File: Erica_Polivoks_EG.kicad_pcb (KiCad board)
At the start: 2 copper layers, 40.3 x 106 mm, 92 parts, among them J1 GATE IN, J2 INV EG OUT, J3 Eurorack_Power_10pin_Unshroud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, J4 GATE DELAY OUT, J5 EG OUT, Q1 2N3904, Q2 2N3904, Q3 2N3904, Q4 2N3904, Q5 2N3904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

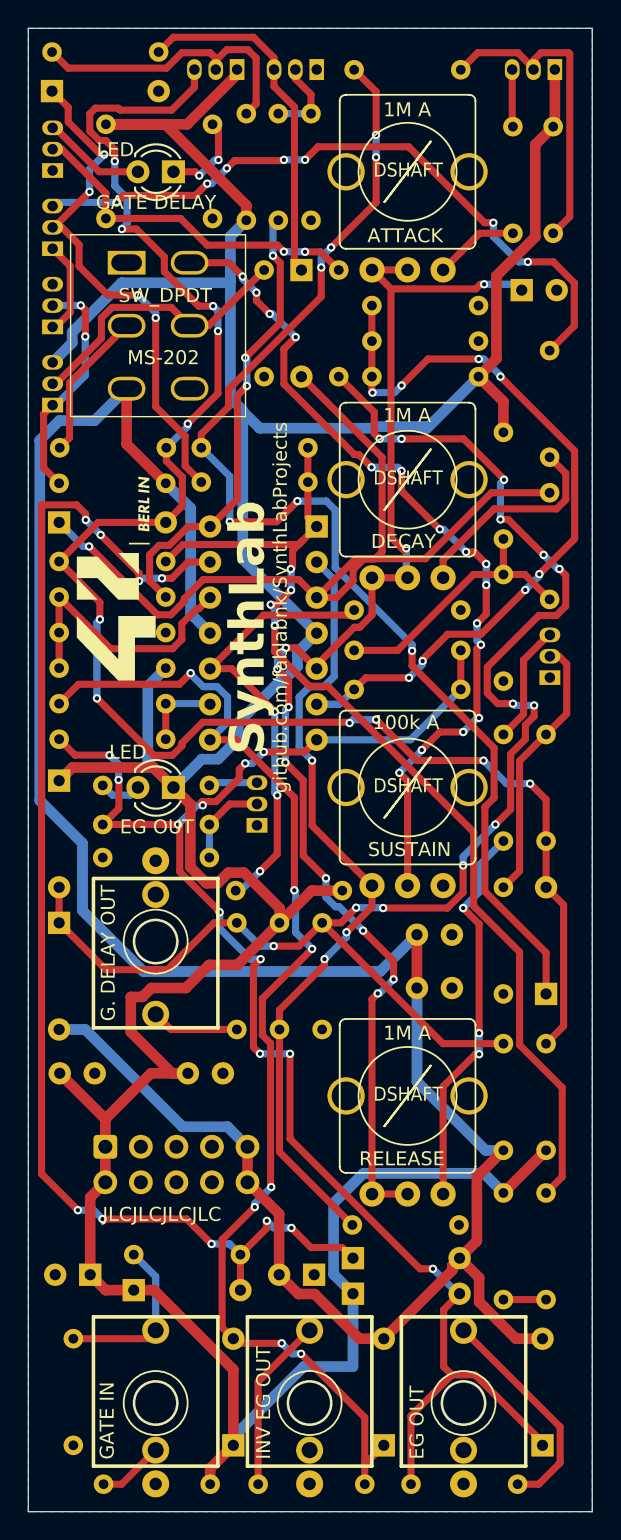
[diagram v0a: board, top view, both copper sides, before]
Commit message: rerouting complete and passes DRC
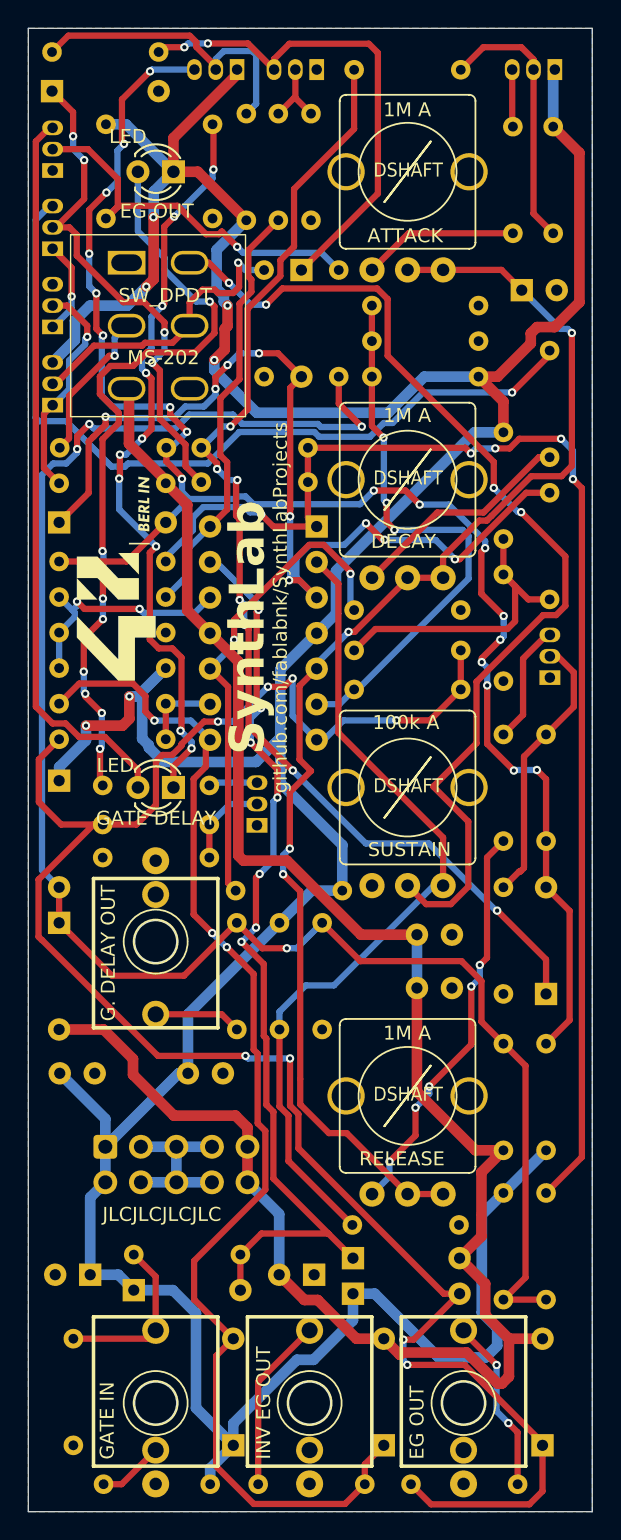
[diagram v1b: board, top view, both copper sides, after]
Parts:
- moved D11 44.0 mm to (60.1, 105.0)
- moved D18 44.0 mm to (60.1, 61.0)
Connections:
- R16 pad 2: Net-(R16-Pad2) -> Net-(D12-K)
- R28 pad 2: Net-(R16-Pad2) -> Net-(D12-K)
- RV1 pad 1: Net-(U1B-+) -> Net-(R1-Pad1)
- RV1 pad 3: Net-(R1-Pad1) -> Net-(U1B-+)
- RV2 pad 1: Net-(U1B-+) -> Net-(R2-Pad1)
- RV2 pad 3: Net-(R2-Pad1) -> Net-(U1B-+)
- RV3 pad 1: Net-(U1B-+) -> Net-(R3-Pad1)
- RV3 pad 3: Net-(R3-Pad1) -> Net-(U1B-+)
- RV4 pad 1: Net-(U1A--) -> GND
- RV4 pad 3: GND -> Net-(U1A--)
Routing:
- net Net-(D18-K): track 3.03 -> 55.5 mm, vias 0 -> 9
- net Net-(D11-A): track 6.52 -> 54.7 mm, vias 2 -> 10
- net Net-(D11-K): track 7.39 -> 52.4 mm
- net -12V: track 170.8 -> 140.7 mm
- net Net-(D1-K): track 92.8 -> 66.5 mm, vias 9 -> 7
- net Net-(D14-K): track 111.9 -> 137.3 mm, vias 11 -> 8
- net Net-(R20-Pad2): track 75.4 -> 93.8 mm, vias 4 -> 5
- net Net-(D12-K): track 108.7 -> 127.1 mm, vias 13 -> 4
- net Net-(U1B--): track 54.3 -> 39.8 mm, vias 8 -> 3
- net Net-(SW1B-A): track 61.8 -> 74.5 mm, vias 16 -> 4
- net GND: track 0.00 -> 12.7 mm
- net Net-(D3-K): track 25.3 -> 36.0 mm, vias 0 -> 2
- net Net-(Q3-C): track 49.2 -> 57.8 mm, vias 7 -> 1
- net Net-(D3-A): track 64.0 -> 69.3 mm, vias 1 -> 9
- net Net-(R1-Pad1): track 6.07 -> 11.2 mm
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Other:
- board text added: "V1.2"
- board text removed: "V1.1"
